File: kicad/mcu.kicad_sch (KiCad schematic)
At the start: 5 parts, among them J10 Conn_01x04_Male, SW1 SW_Push, U4 ESP32DevKitCV4

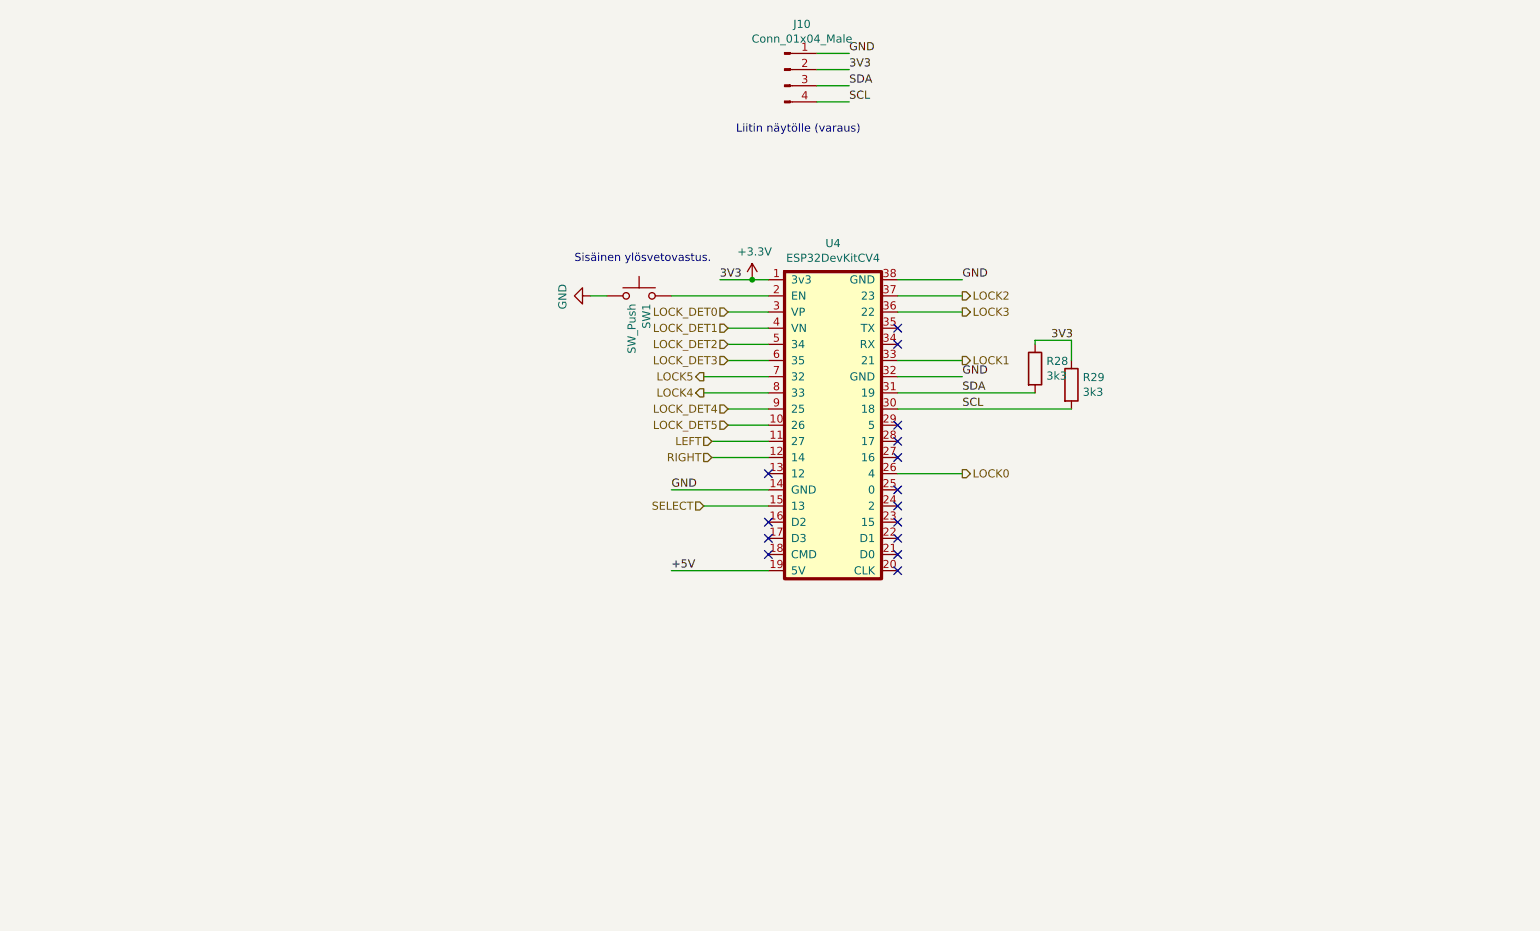
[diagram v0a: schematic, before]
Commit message: Update PCB with IO expander
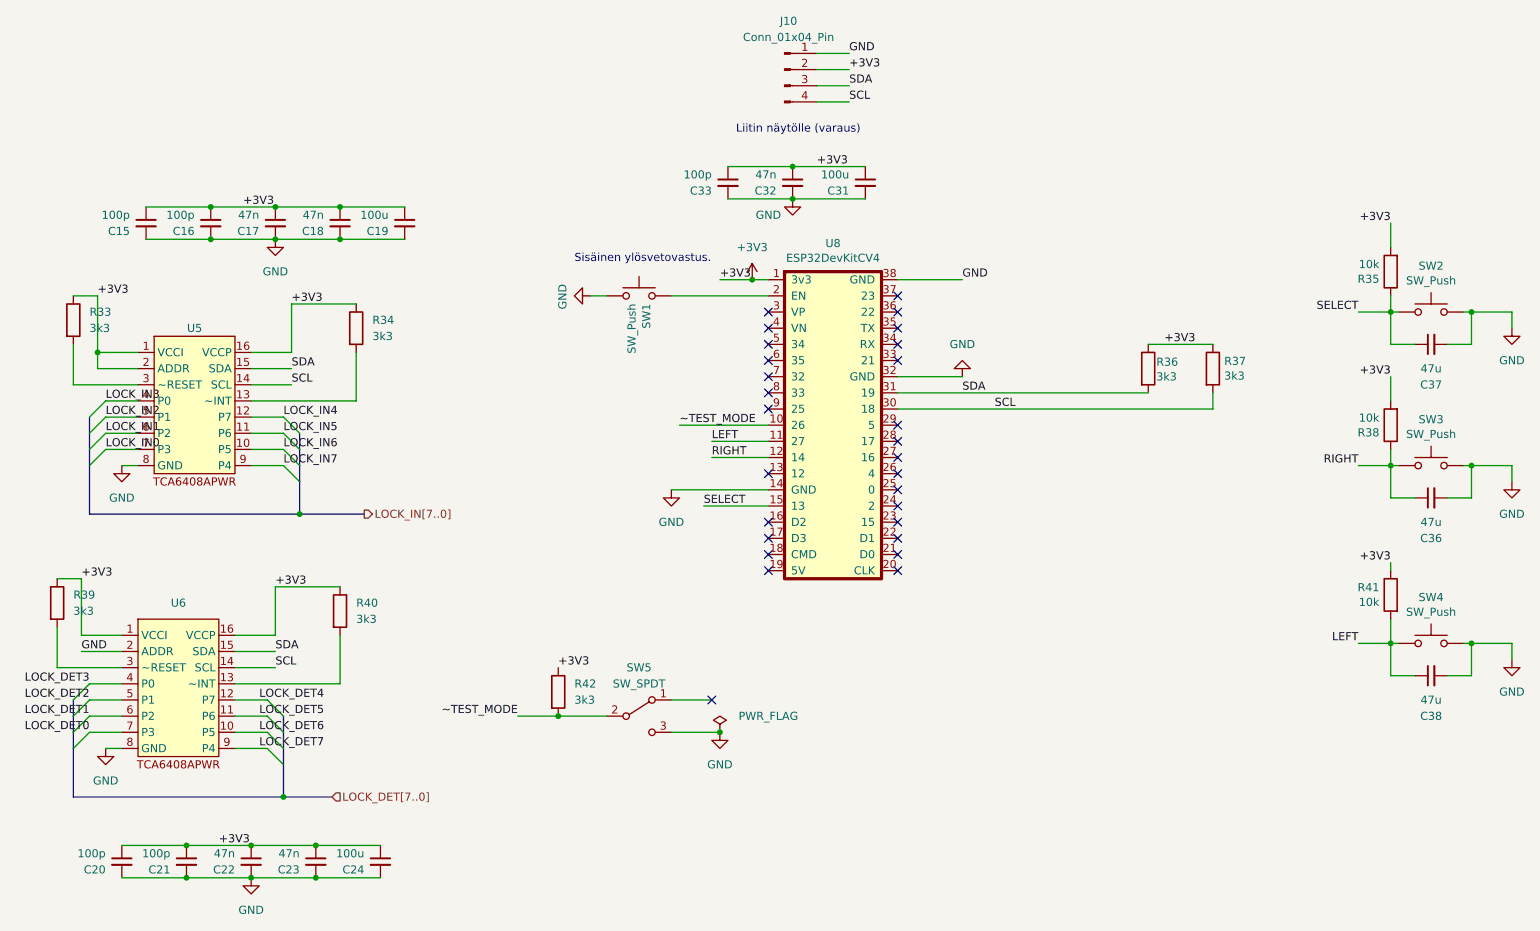
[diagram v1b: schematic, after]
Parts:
- removed J10: Conn_01x04_Male, Connector_PinHeader_2.00mm:PinHeader_1x04_P2.00mm_Vertical, symbol Connector:Conn_01x04_Male
- added C15, C16, C20, C21, C33: 100p, Capacitor_SMD:C_0805_2012Metric_Pad1.18x1.45mm_HandSolder, symbol Device:C_Small
- added C17, C18, C22, C23, C32: 47n, Capacitor_SMD:C_0805_2012Metric_Pad1.18x1.45mm_HandSolder, symbol Device:C_Small
- added C19, C24, C31: 100u, Capacitor_THT:CP_Radial_D5.0mm_P2.50mm, symbol Device:C_Small
- added C36, C37, C38: 47u, Capacitor_SMD:C_0805_2012Metric_Pad1.18x1.45mm_HandSolder, symbol Device:C_Small
- added J10: Conn_01x04_Pin, Connector_PinHeader_2.00mm:PinHeader_1x04_P2.00mm_Vertical, symbol Connector:Conn_01x04_Pin
- added R33, R34, R39, R40, R42: 3k3, Resistor_SMD:R_0805_2012Metric_Pad1.20x1.40mm_HandSolder, symbol Device:R
- added R35, R38, R41: 10k, Resistor_SMD:R_0805_2012Metric_Pad1.20x1.40mm_HandSolder, symbol Device:R
- added SW2, SW3, SW4: SW_Push, Connector_PinHeader_2.54mm:PinHeader_1x02_P2.54mm_Vertical, symbol Switch:SW_Push
- added SW5: SW_SPDT, Connector_TE-Connectivity:TE_826576-3_1x03_P3.96mm_Vertical, symbol Switch:SW_SPDT
- added U5, U6: ~, Package_SO:TSSOP-16_4.4x5mm_P0.65mm, symbol Interface_Expansion:TCA6408APWR
- R36: renamed from R28; footprint Resistor_SMD:R_0805_2012Metric_Pad1.15x1.40mm_HandSolder -> Resistor_SMD:R_0805_2012Metric_Pad1.20x1.40mm_HandSolder
- R37: renamed from R29; footprint Resistor_SMD:R_0805_2012Metric_Pad1.15x1.40mm_HandSolder -> Resistor_SMD:R_0805_2012Metric_Pad1.20x1.40mm_HandSolder
- renumbered U4 to U8
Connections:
- net +3V3: now also C15.1, C16.1, C17.1, C18.1, C19.1, C20.1, C21.1, C22.1, C23.1, C24.1, C31.1, C32.1, C33.1, J10.2 (Pin_2), R33.1, R34.1, R35.2, R38.2, R39.1, R40.1, R41.1, R42.1, U5.1 (VCCI), U5.16 (VCCP), U5.2 (ADDR), U6.1 (VCCI), U6.16 (VCCP)
- net GND: now also C15.2, C16.2, C17.2, C18.2, C19.2, C20.2, C21.2, C22.2, C23.2, C24.2, C31.2, C32.2, C33.2, C36.2, C37.2, C38.2, J10.1 (Pin_1), SW2.1, SW3.1, SW4.1, SW5.3 (C), U5.8 (GND), U6.2 (ADDR), U6.8 (GND)
- net LEFT: now also C38.1, R41.2, SW4.2
- net LOCK_DET0: now also U6.7 (P3); no longer U8.3 (VP)
- net LOCK_DET1: now also U6.6 (P2); no longer U8.4 (VN)
- net LOCK_DET2: now also U6.5 (P1); no longer U8.5 (34)
- net LOCK_DET3: now also U6.4 (P0); no longer U8.6 (35)
- net LOCK_DET4: now also U6.12 (P7); no longer U8.9 (25)
- net LOCK_DET5: now also U6.11 (P6); no longer U8.10 (26)
- net RIGHT: now also C36.1, R38.1, SW3.2
- net SCL: now also J10.4 (Pin_4), U5.14 (SCL), U6.14 (SCL)
- net SDA: now also J10.3 (Pin_3), U5.15 (SDA), U6.15 (SDA)
- net SELECT: now also C37.1, R35.1, SW2.2
- net +5V: no longer names the net of U8.19 (5V)
- net LOCK0: no longer names the net of U8.26 (4)
- net LOCK1: no longer names the net of U8.33 (21)
- net LOCK2: no longer names the net of U8.37 (23)
- net LOCK3: no longer names the net of U8.36 (22)
- net LOCK4: no longer names the net of U8.8 (33)
- net LOCK5: no longer names the net of U8.7 (32)
- new net: R39.2, U6.3 (~RESET)
- new net: R34.2, U5.13 (~INT)
- new net: R33.2, U5.3 (~RESET)
- new net: R40.2, U6.13 (~INT)
- new net LOCK_DET6: U6.10 (P5)
- new net LOCK_DET7: U6.9 (P4)
- new net LOCK_IN0: U5.7 (P3)
- new net LOCK_IN1: U5.6 (P2)
- new net LOCK_IN2: U5.5 (P1)
- new net LOCK_IN3: U5.4 (P0)
- new net LOCK_IN4: U5.12 (P7)
- new net LOCK_IN5: U5.11 (P6)
- new net LOCK_IN6: U5.10 (P5)
- new net LOCK_IN7: U5.9 (P4)
- new net ~TEST_MODE: R42.2, SW5.2 (B), U8.10 (26)
- no-connect marks 15 -> 28
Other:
- moved on the sheet: R36, R37

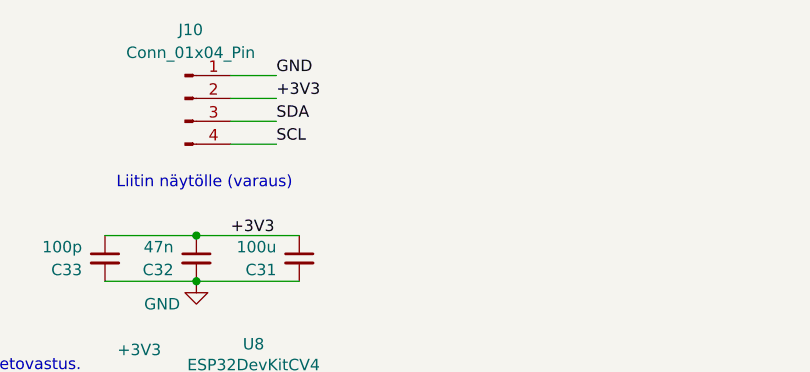
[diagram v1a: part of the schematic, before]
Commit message: Fix remaining DRC + ERC, ready for manufacturing
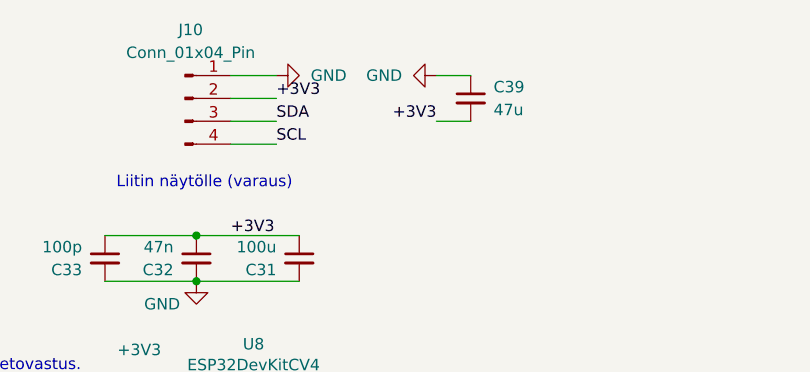
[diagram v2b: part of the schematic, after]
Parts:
- added C39: 47u, Capacitor_SMD:C_0805_2012Metric_Pad1.18x1.45mm_HandSolder, symbol Device:C_Small
- U8: footprint devkits:ESP32_DevkitC_ExtraPins -> devkits:ESP32-DevkitC
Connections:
- net +3V3: now also C39.2
- net GND: now also C39.1
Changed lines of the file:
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@@
+    (stroke (width 0) (type default))
+  )
+  (wire (pts (xy 175.26 45.72) (xy 179.07 45.72))
     (stroke (width 0) (type default))
   )
@@
     (stroke (width 0) (type default))
   )
+  (wire (pts (xy 175.26 50.8) (xy 179.07 50.8))
+    (stroke (width 0) (type default))
+  )
   (wire (pts (xy 251.46 91.44) (xy 255.27 91.44))
     (stroke (width 0) (type default))
@@
   (label "+3V3" (at 67.31 129.54 0) (fields_autoplaced)
     (effects (font (size 1.27 1.27)) (justify left bottom))
+  )
+  (label "+3V3" (at 175.26 50.8 180) (fields_autoplaced)
+    (effects (font (size 1.27 1.27)) (justify right bottom))
   )
   (label "LEFT" (at 135.89 106.68 0) (fields_autoplaced)
@@
     (effects (font (size 1.27 1.27)) (justify left bottom))
   )
-  (label "GND" (at 157.48 45.72 0) (fields_autoplaced)
-    (effects (font (size 1.27 1.27)) (justify left bottom))
-  )
   (label "+3V3" (at 207.01 91.44 0) (fields_autoplaced)
     (effects (font (size 1.27 1.27)) (justify left bottom))
@@
       (effects (font (size 1.27 1.27)))
     )
-    (property "Footprint" "devkits:ESP32_DevkitC_ExtraPins" (at 156.21 104.14 0)
+    (property "Footprint" "devkits:ESP32-DevkitC" (at 156.21 104.14 0)
       (effects (font (size 1.27 1.27)) hide)
     )
@@
     )
   )
+  (symbol (lib_id "Device:C_Small") (at 179.07 48.26 0) (unit 1)
+    (in_bom yes) (on_board yes) (dnp no) (fields_autoplaced)
+    (property "Reference" "C39" (at 181.61 46.9963 0)
+      (effects (font (size 1.27 1.27)) (justify left))
+    )
+    (property "Value" "47u" (at 181.61 49.5363 0)
+      (effects (font (size 1.27 1.27)) (justify left))
+    )
+    (property "Footprint" "Capacitor_SMD:C_0805_2012Metric_Pad1.18x1.45mm_HandSolder" (at 179.07 48.26 0)
+      (effects (font (size 1.27 1.27)) hide)
+    )
+    (property "Datasheet" "~" (at 179.07 48.26 0)
+      (effects (font (size 1.27 1.27)) hide)
+    )
+    (pin "1")
+    (pin "2")
+    (instances
+      (project "horse_feeder"
+        (path "/6475547d-3216-45a4-a15c-48314f1dd0f9/1a60710e-d81d-42ec-a916-c92b42f75637"
+          (reference "C39") (unit 1)
+        )
+      )
+    )
+  )
   (symbol (lib_id "Device:R") (at 33.02 132.08 0) (unit 1)
     (in_bom yes) (on_board yes) (dnp no) (fields_autoplaced)
@@
     )
   )
+  (symbol (lib_id "power:GND") (at 175.26 45.72 270) (unit 1)
+    (in_bom yes) (on_board yes) (dnp no) (fields_autoplaced)
+    (property "Reference" "#PWR058" (at 168.91 45.72 0)
+      (effects (font (size 1.27 1.27)) hide)
+    )
+    (property "Value" "GND" (at 171.45 45.72 90)
+      (effects (font (size 1.27 1.27)) (justify right))
+    )
+    (property "Footprint" "" (at 175.26 45.72 0)
+      (effects (font (size 1.27 1.27)) hide)
+    )
+    (property "Datasheet" "" (at 175.26 45.72 0)
+      (effects (font (size 1.27 1.27)) hide)
+    )
+    (pin "1")
+    (instances
+      (project "horse_feeder"
+        (path "/6475547d-3216-45a4-a15c-48314f1dd0f9/1a60710e-d81d-42ec-a916-c92b42f75637"
+          (reference "#PWR058") (unit 1)
+        )
+      )
+    )
+  )
   (symbol (lib_id "Device:C_Small") (at 43.18 172.72 0) (unit 1)
     (in_bom yes) (on_board yes) (dnp no)
@@
         )
       )
+    )
+  )
+  (symbol (lib_id "power:GND") (at 157.48 45.72 90) (unit 1)
+    (in_bom yes) (on_board yes) (dnp no) (fields_autoplaced)
+    (property "Reference" "#PWR057" (at 163.83 45.72 0)
+      (effects (font (size 1.27 1.27)) hide)
+    )
+    (property "Value" "GND" (at 161.29 45.72 90)
+      (effects (font (size 1.27 1.27)) (justify right))
+    )
+    (property "Footprint" "" (at 157.48 45.72 0)
+      (effects (font (size 1.27 1.27)) hide)
+    )
+    (property "Datasheet" "" (at 157.48 45.72 0)
+      (effects (font (size 1.27 1.27)) hide)
+    )
+    (pin "1")
+    (instances
+      (project "horse_feeder"
+        (path "/6475547d-3216-45a4-a15c-48314f1dd0f9/1a60710e-d81d-42ec-a916-c92b42f75637"
+          (reference "#PWR057") (unit 1)
+        )
+      )
